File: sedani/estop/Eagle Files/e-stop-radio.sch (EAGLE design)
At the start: 37 parts, among them J1 E-STOP HEADER, J2 AVR_SPI_PROG_3X2PTH, J3 Buttons, U1 RFM69HCW, U2 TPS62203DBVR, U3 CD40109BPWR, X1 8 MHz, X2 uFL/SMA

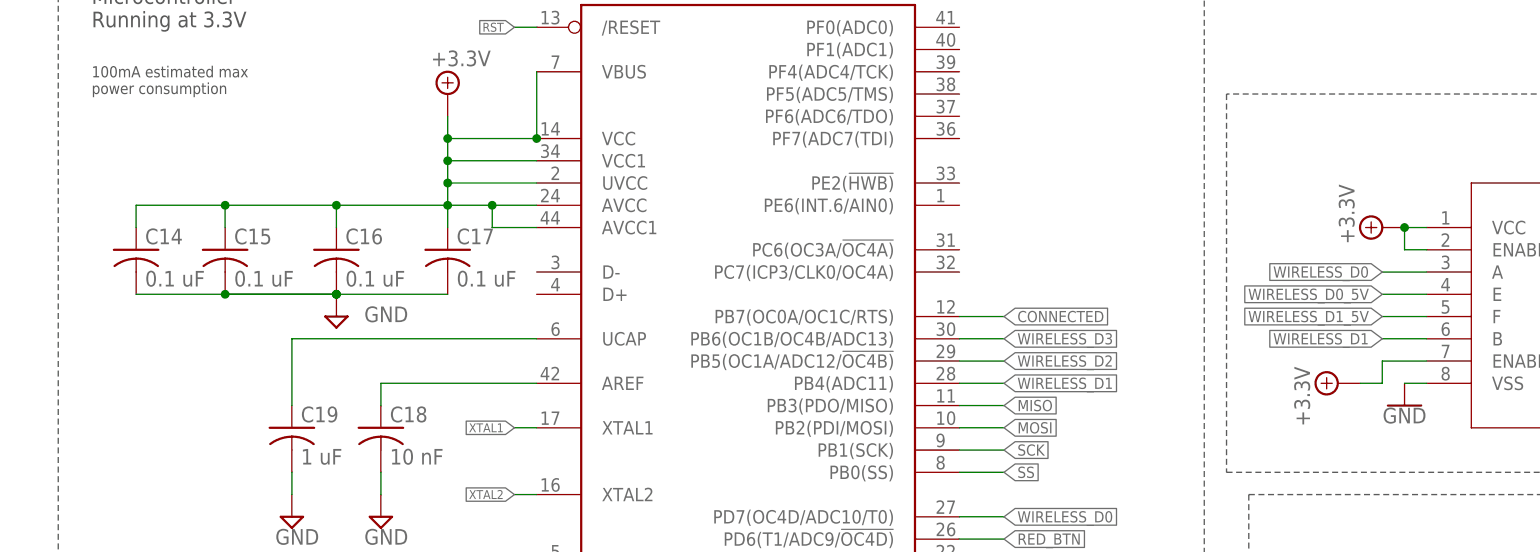
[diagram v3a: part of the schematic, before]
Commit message: partially routed, but going to shrink dimensions
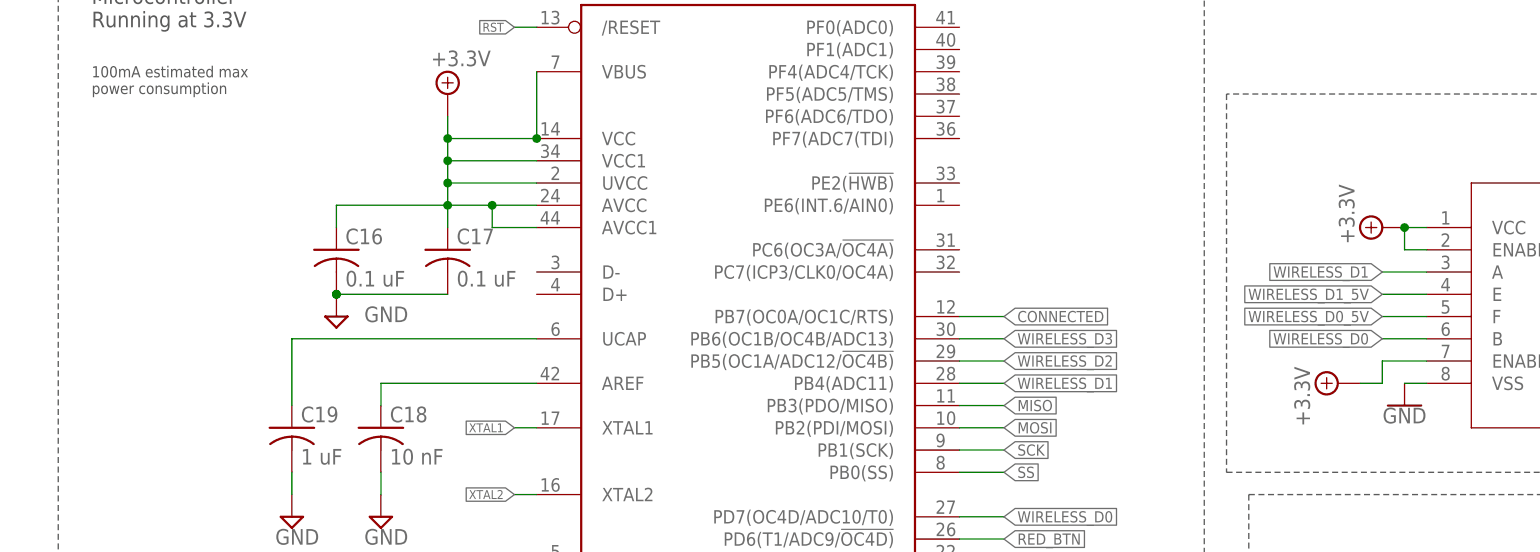
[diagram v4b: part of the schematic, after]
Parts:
- removed C14, C15: 0.1 uF, resistor:C-USC0603
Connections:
- net +3.3V: no longer C14.1, C15.1
- net GND: no longer C14.2, C15.2
- net WIRELESS_D0: now also U3.B; no longer U3.A
- net WIRELESS_D0_5V: now also U3.F; no longer U3.E
- net WIRELESS_D1: now also U3.A; no longer U3.B
- net WIRELESS_D1_5V: now also U3.E; no longer U3.F
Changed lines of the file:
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@@
 </variantdefs>
 <classes>
-<class number="0" name="default" width="0.2032" drill="0">
+<class number="0" name="default" width="0.3048" drill="0.508">
 </class>
 <class number="1" name="power" width="0.4064" drill="0.508">
 </class>
-<class number="2" name="RF" width="0.2032" drill="0">
+<class number="2" name="RF" width="0.3048" drill="0">
 </class>
 </classes>
@@
 <part name="SUPPLY54" library="supply2" library_urn="urn:adsk.eagle:library:372" deviceset="GND" device=""/>
 <part name="C16" library="resistor" library_urn="urn:adsk.eagle:library:348" deviceset="C-US" device="C0603" package3d_urn="urn:adsk.eagle:package:23616/2" value="0.1 uF"/>
-<part name="C15" library="resistor" library_urn="urn:adsk.eagle:library:348" deviceset="C-US" device="C0603" package3d_urn="urn:adsk.eagle:package:23616/2" value="0.1 uF"/>
-<part name="C14" library="resistor" library_urn="urn:adsk.eagle:library:348" deviceset="C-US" device="C0603" package3d_urn="urn:adsk.eagle:package:23616/2" value="0.1 uF"/>
 <part name="X1" library="estop-v1.0" deviceset="ECS-80-18-5PX-TR" device="" value="8 MHz"/>
 <part name="SUPPLY1" library="RoboJackets-Supplies" deviceset="+3.3V" device=""/>
@@
 <attribute name="VALUE" x="46.736" y="23.749" size="1.778" layer="96"/>
 </instance>
-<instance part="C15" gate="G$1" x="33.02" y="27.94" smashed="yes">
-<attribute name="NAME" x="34.036" y="28.575" size="1.778" layer="95"/>
-<attribute name="VALUE" x="34.036" y="23.749" size="1.778" layer="96"/>
-</instance>
-<instance part="C14" gate="G$1" x="22.86" y="27.94" smashed="yes">
-<attribute name="NAME" x="23.876" y="28.575" size="1.778" layer="95"/>
-<attribute name="VALUE" x="23.876" y="23.749" size="1.778" layer="96"/>
-</instance>
 <instance part="X1" gate="G$1" x="40.64" y="86.36" smashed="yes">
 <attribute name="VALUE" x="38.1" y="88.9" size="1.778" layer="96"/>
@@
 <pinref part="C17" gate="G$1" pin="2"/>
 <pinref part="SUPPLY54" gate="GND" pin="GND"/>
-<pinref part="C14" gate="G$1" pin="2"/>
-<pinref part="C15" gate="G$1" pin="2"/>
 <pinref part="C16" gate="G$1" pin="2"/>
-<wire x1="33.02" y1="22.86" x2="45.72" y2="22.86" width="0.1524" layer="91"/>
-<junction x="33.02" y="22.86"/>
 <junction x="45.72" y="22.86"/>
 <junction x="45.72" y="22.86"/>
 <wire x1="45.72" y1="22.86" x2="58.42" y2="22.86" width="0.1524" layer="91"/>
-<wire x1="45.72" y1="22.86" x2="22.86" y2="22.86" width="0.1524" layer="91"/>
 </segment>
 <segment>
@@
 <wire x1="63.5" y1="30.48" x2="68.58" y2="30.48" width="0.1524" layer="91"/>
 <wire x1="58.42" y1="33.02" x2="45.72" y2="33.02" width="0.1524" layer="91"/>
-<pinref part="C14" gate="G$1" pin="1"/>
-<wire x1="45.72" y1="33.02" x2="33.02" y2="33.02" width="0.1524" layer="91"/>
-<wire x1="33.02" y1="33.02" x2="22.86" y2="33.02" width="0.1524" layer="91"/>
-<wire x1="22.86" y1="33.02" x2="22.86" y2="30.48" width="0.1524" layer="91"/>
-<pinref part="C15" gate="G$1" pin="1"/>
-<wire x1="33.02" y1="30.48" x2="33.02" y2="33.02" width="0.1524" layer="91"/>
-<junction x="33.02" y="33.02"/>
 <pinref part="C16" gate="G$1" pin="1"/>
 <wire x1="45.72" y1="30.48" x2="45.72" y2="33.02" width="0.1524" layer="91"/>
-<junction x="45.72" y="33.02"/>
 <wire x1="63.5" y1="30.48" x2="63.5" y2="33.02" width="0.1524" layer="91"/>
 <junction x="63.5" y="33.02"/>
@@
 <net name="WIRELESS_D1" class="0">
 <segment>
-<wire x1="170.18" y1="17.78" x2="165.1" y2="17.78" width="0.1524" layer="91"/>
-<label x="165.1" y="17.78" size="1.27" layer="95" font="vector" rot="MR0" xref="yes"/>
-<pinref part="U3" gate="A" pin="B"/>
-</segment>
-<segment>
 <wire x1="116.84" y1="12.7" x2="121.92" y2="12.7" width="0.1524" layer="91"/>
 <label x="121.92" y="12.7" size="1.27" layer="95" font="vector" xref="yes"/>
 <pinref part="MC1" gate="G$1" pin="PB4(ADC11)"/>
 </segment>
+<segment>
+<pinref part="U3" gate="A" pin="A"/>
+<wire x1="170.18" y1="25.4" x2="165.1" y2="25.4" width="0.1524" layer="91"/>
+<label x="165.1" y="25.4" size="1.27" layer="95" font="vector" rot="R180" xref="yes"/>
+</segment>
 </net>
 <net name="WIRELESS_D0" class="0">
-<segment>
-<wire x1="170.18" y1="25.4" x2="165.1" y2="25.4" width="0.1524" layer="91"/>
-<label x="165.1" y="25.4" size="1.27" layer="95" font="vector" rot="MR0" xref="yes"/>
-<pinref part="U3" gate="A" pin="A"/>
-</segment>
 <segment>
 <wire x1="116.84" y1="-2.54" x2="121.92" y2="-2.54" width="0.1524" layer="91"/>
 <label x="121.92" y="-2.54" size="1.27" layer="95" font="vector" xref="yes"/>
 <pinref part="MC1" gate="G$1" pin="PD7(OC4D/ADC10/T0)"/>
+</segment>
+<segment>
+<pinref part="U3" gate="A" pin="B"/>
+<wire x1="170.18" y1="17.78" x2="165.1" y2="17.78" width="0.1524" layer="91"/>
+<label x="165.1" y="17.78" size="1.27" layer="95" font="vector" rot="R180" xref="yes"/>
 </segment>
 </net>
@@
 <net name="WIRELESS_D1_5V" class="0">
 <segment>
-<wire x1="170.18" y1="20.32" x2="165.1" y2="20.32" width="0.1524" layer="91"/>
-<label x="165.1" y="20.32" size="1.27" layer="95" font="vector" rot="MR0" xref="yes"/>
-<pinref part="U3" gate="A" pin="F"/>
-</segment>
-<segment>
 <label x="154.94" y="81.28" size="1.27" layer="95" font="vector" rot="MR0" xref="yes"/>
 <pinref part="R8" gate="G$1" pin="1"/>
 <wire x1="175.26" y1="81.28" x2="154.94" y2="81.28" width="0.1524" layer="91"/>
 </segment>
+<segment>
+<pinref part="U3" gate="A" pin="E"/>
+<wire x1="170.18" y1="22.86" x2="165.1" y2="22.86" width="0.1524" layer="91"/>
+<label x="165.1" y="22.86" size="1.27" layer="95" font="vector" rot="R180" xref="yes"/>
+</segment>
 </net>
 <net name="WIRELESS_D0_5V" class="0">
-<segment>
-<wire x1="170.18" y1="22.86" x2="165.1" y2="22.86" width="0.1524" layer="91"/>
-<label x="165.1" y="22.86" size="1.27" layer="95" font="vector" rot="MR0" xref="yes"/>
-<pinref part="U3" gate="A" pin="E"/>
-</segment>
 <segment>
 <label x="154.94" y="78.74" size="1.27" layer="95" font="vector" rot="MR0" xref="yes"/>
@@
 <wire x1="165.1" y1="78.74" x2="154.94" y2="78.74" width="0.1524" layer="91"/>
 </segment>
-</net>
+<segment>
+<pinref part="U3" gate="A" pin="F"/>
+<wire x1="170.18" y1="20.32" x2="165.1" y2="20.32" width="0.1524" layer="91"/>
+<label x="165.1" y="20.32" size="1.27" layer="95" font="vector" rot="R180" xref="yes"/>
+</segment>
+</net>

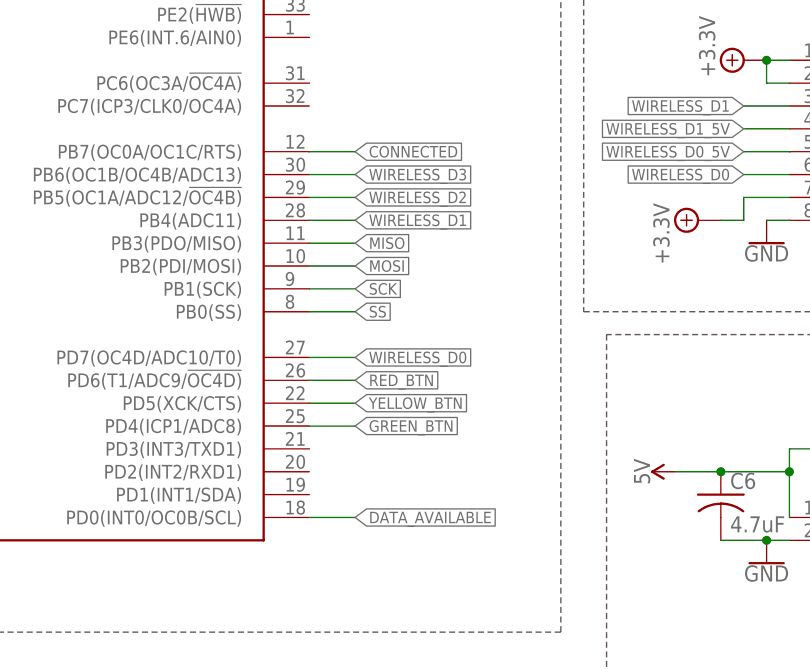
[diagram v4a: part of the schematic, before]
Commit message: partially layed out. Need to change SMA connector
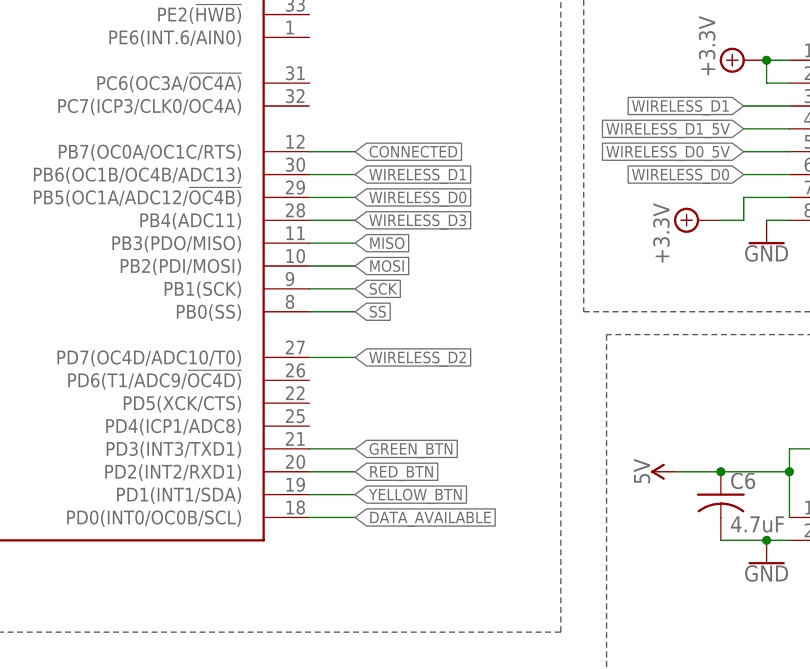
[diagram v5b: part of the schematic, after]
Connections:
- net GREEN_BTN: now also MC1.PD3(INT3/TXD1); no longer MC1.PD4(ICP1/ADC8)
- net RED_BTN: now also MC1.PD2(INT2/RXD1); no longer MC1.PD6(T1/ADC9/!OC4D)
- net WIRELESS_D0: now also MC1.PB5(OC1A/ADC12/!OC4B); no longer MC1.PD7(OC4D/ADC10/T0)
- net WIRELESS_D1: now also MC1.PB6(OC1B/OC4B/ADC13); no longer MC1.PB4(ADC11)
- net WIRELESS_D2: now also MC1.PD7(OC4D/ADC10/T0); no longer MC1.PB5(OC1A/ADC12/!OC4B)
- net WIRELESS_D3: now also MC1.PB4(ADC11); no longer MC1.PB6(OC1B/OC4B/ADC13)
- net YELLOW_BTN: now also MC1.PD1(INT1/SDA); no longer MC1.PD5(XCK/CTS)
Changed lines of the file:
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@@
+</segment>
+<segment>
+<wire x1="116.84" y1="12.7" x2="121.92" y2="12.7" width="0.1524" layer="91"/>
+<label x="121.92" y="12.7" size="1.27" layer="95" font="vector" xref="yes"/>
+<pinref part="MC1" gate="G$1" pin="PB4(ADC11)"/>
+</segment>
+</net>
+<net name="WIRELESS_D2" class="0">
+<segment>
+<wire x1="236.22" y1="15.24" x2="241.3" y2="15.24" width="0.1524" layer="91"/>
+<label x="241.3" y="15.24" size="1.27" layer="95" font="vector" xref="yes"/>
+<pinref part="U3" gate="A" pin="C"/>
+</segment>
+<segment>
+<wire x1="116.84" y1="-2.54" x2="121.92" y2="-2.54" width="0.1524" layer="91"/>
+<label x="121.92" y="-2.54" size="1.27" layer="95" font="vector" xref="yes"/>
+<pinref part="MC1" gate="G$1" pin="PD7(OC4D/ADC10/T0)"/>
+</segment>
+</net>
+<net name="WIRELESS_D1" class="0">
+<segment>
+<pinref part="U3" gate="A" pin="A"/>
+<wire x1="170.18" y1="25.4" x2="165.1" y2="25.4" width="0.1524" layer="91"/>
+<label x="165.1" y="25.4" size="1.27" layer="95" font="vector" rot="R180" xref="yes"/>
 </segment>
 <segment>
@@
 </segment>
 </net>
-<net name="WIRELESS_D2" class="0">
-<segment>
-<wire x1="236.22" y1="15.24" x2="241.3" y2="15.24" width="0.1524" layer="91"/>
-<label x="241.3" y="15.24" size="1.27" layer="95" font="vector" xref="yes"/>
-<pinref part="U3" gate="A" pin="C"/>
+<net name="WIRELESS_D0" class="0">
+<segment>
+<pinref part="U3" gate="A" pin="B"/>
+<wire x1="170.18" y1="17.78" x2="165.1" y2="17.78" width="0.1524" layer="91"/>
+<label x="165.1" y="17.78" size="1.27" layer="95" font="vector" rot="R180" xref="yes"/>
 </segment>
 <segment>
@@
 <label x="121.92" y="15.24" size="1.27" layer="95" font="vector" xref="yes"/>
 <pinref part="MC1" gate="G$1" pin="PB5(OC1A/ADC12/!OC4B)"/>
-</segment>
-</net>
-<net name="WIRELESS_D1" class="0">
-<segment>
-<wire x1="116.84" y1="12.7" x2="121.92" y2="12.7" width="0.1524" layer="91"/>
-<label x="121.92" y="12.7" size="1.27" layer="95" font="vector" xref="yes"/>
-<pinref part="MC1" gate="G$1" pin="PB4(ADC11)"/>
-</segment>
-<segment>
-<pinref part="U3" gate="A" pin="A"/>
-<wire x1="170.18" y1="25.4" x2="165.1" y2="25.4" width="0.1524" layer="91"/>
-<label x="165.1" y="25.4" size="1.27" layer="95" font="vector" rot="R180" xref="yes"/>
-</segment>
-</net>
-<net name="WIRELESS_D0" class="0">
-<segment>
-<wire x1="116.84" y1="-2.54" x2="121.92" y2="-2.54" width="0.1524" layer="91"/>
-<label x="121.92" y="-2.54" size="1.27" layer="95" font="vector" xref="yes"/>
-<pinref part="MC1" gate="G$1" pin="PD7(OC4D/ADC10/T0)"/>
-</segment>
-<segment>
-<pinref part="U3" gate="A" pin="B"/>
-<wire x1="170.18" y1="17.78" x2="165.1" y2="17.78" width="0.1524" layer="91"/>
-<label x="165.1" y="17.78" size="1.27" layer="95" font="vector" rot="R180" xref="yes"/>
 </segment>
 </net>
@@
 </segment>
 </net>
-<net name="N$1" class="0">
+<net name="N$1" class="1">
 <segment>
 <pinref part="U2" gate="A" pin="SW"/>
@@
 </segment>
 <segment>
-<wire x1="116.84" y1="-10.16" x2="121.92" y2="-10.16" width="0.1524" layer="91"/>
-<label x="121.92" y="-10.16" size="1.27" layer="95" font="vector" xref="yes"/>
-<pinref part="MC1" gate="G$1" pin="PD4(ICP1/ADC8)"/>
+<wire x1="116.84" y1="-12.7" x2="121.92" y2="-12.7" width="0.1524" layer="91"/>
+<label x="121.92" y="-12.7" size="1.27" layer="95" font="vector" xref="yes"/>
+<pinref part="MC1" gate="G$1" pin="PD3(INT3/TXD1)"/>
 </segment>
 </net>
@@
 </segment>
 <segment>
-<wire x1="116.84" y1="-5.08" x2="121.92" y2="-5.08" width="0.1524" layer="91"/>
-<label x="121.92" y="-5.08" size="1.27" layer="95" font="vector" xref="yes"/>
-<pinref part="MC1" gate="G$1" pin="PD6(T1/ADC9/!OC4D)"/>
+<wire x1="116.84" y1="-15.24" x2="121.92" y2="-15.24" width="0.1524" layer="91"/>
+<label x="121.92" y="-15.24" size="1.27" layer="95" font="vector" xref="yes"/>
+<pinref part="MC1" gate="G$1" pin="PD2(INT2/RXD1)"/>
 </segment>
 </net>
@@
 </segment>
 <segment>
-<wire x1="116.84" y1="-7.62" x2="121.92" y2="-7.62" width="0.1524" layer="91"/>
-<label x="121.92" y="-7.62" size="1.27" layer="95" font="vector" xref="yes"/>
-<pinref part="MC1" gate="G$1" pin="PD5(XCK/CTS)"/>
-</segment>
-</net>
+<wire x1="116.84" y1="-17.78" x2="121.92" y2="-17.78" width="0.1524" layer="91"/>
+<label x="121.92" y="-17.78" size="1.27" layer="95" font="vector" xref="yes"/>
+<pinref part="MC1" gate="G$1" pin="PD1(INT1/SDA)"/>
+</segment>
+</net>

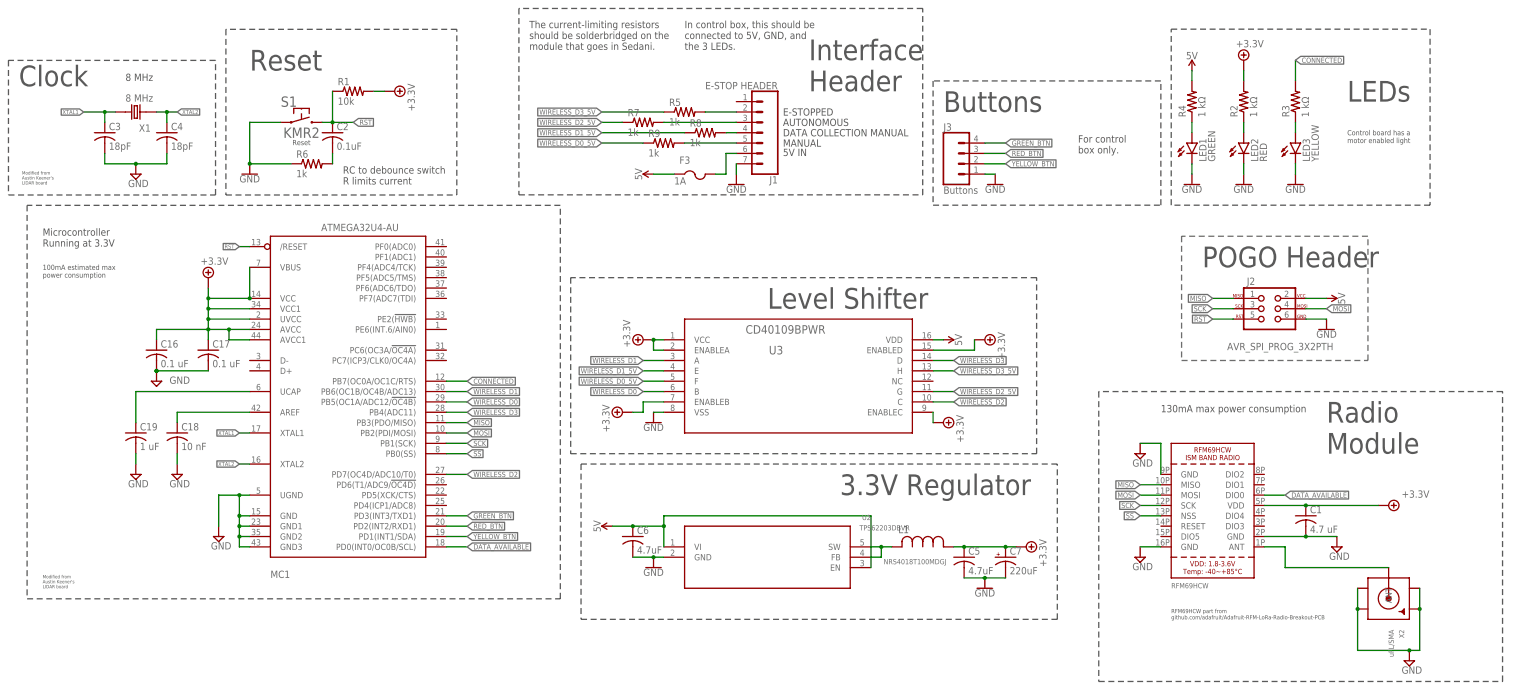
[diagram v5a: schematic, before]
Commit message: changed antenna to right angle and removed crystal
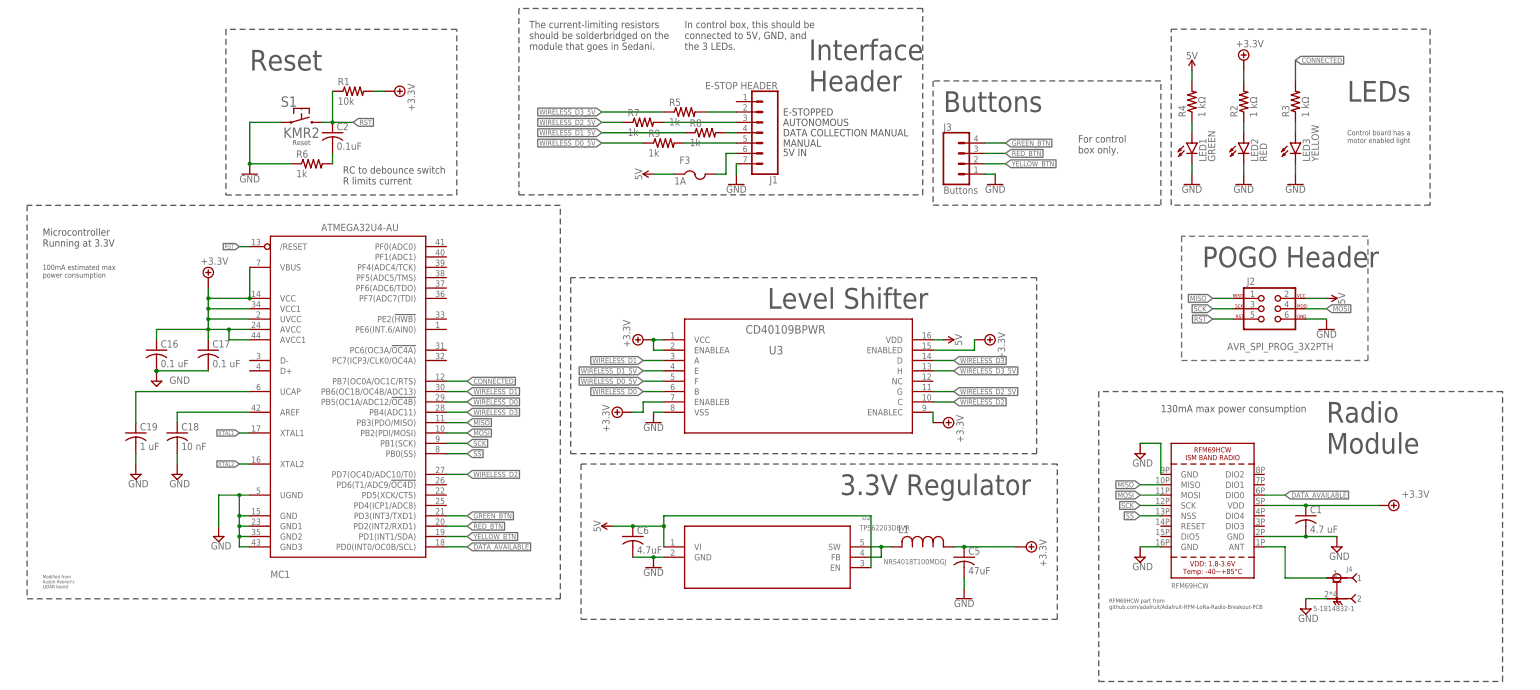
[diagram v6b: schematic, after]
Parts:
- removed C3, C4: 18pF, resistor:C-USC0603
- removed C7: 220uF, rcl:CPOL-USE2.5-7
- removed X1: 8 MHz, estop-v1.0:ECS-80-18-5PX-TR
- removed X2: uFL/SMA, microbuilder:SMACONNECTOR_EDGE_UFL
- added J4: 5-1814832-1, estop-v1.0:5-1814832-1
- C5: value 4.7uF -> 47uF; device rcl:C-USC0603 -> rcl:C-USC1206
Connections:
- net +3.3V: no longer C7.+
- net GND: now also J4.2; no longer C3.2, C4.2, C7.-, X2.GND1, X2.GND2, X2.GND3, X2.GND4
- net RF_SIGNAL: now also J4.1; no longer X2.ANT
- net XTAL1: no longer C3.1, X1.1
- net XTAL2: no longer C4.1, X1.2
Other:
- note removed: "8 MHz"
- note removed: "Clock"
